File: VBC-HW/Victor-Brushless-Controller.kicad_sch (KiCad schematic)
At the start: 79 parts, among them J1 i2c QWIIC, P1 PVDD, P2 GND, Q1 TPH4R008NH, Q2 TPH4R008NH, Q3 TPH4R008NH, Q4 TPH4R008NH, Q5 TPH4R008NH, Q6 TPH4R008NH, SW1 SW_SPST, SW2 SW_SPST, U1 DRV8305NQPHPRQ1, U2 ESP-WROOM-32E, U3 LMR14010ADDCR, U5 STLM20W87F, U6 External SPI, U7 AS5047P-ATSM_C962063

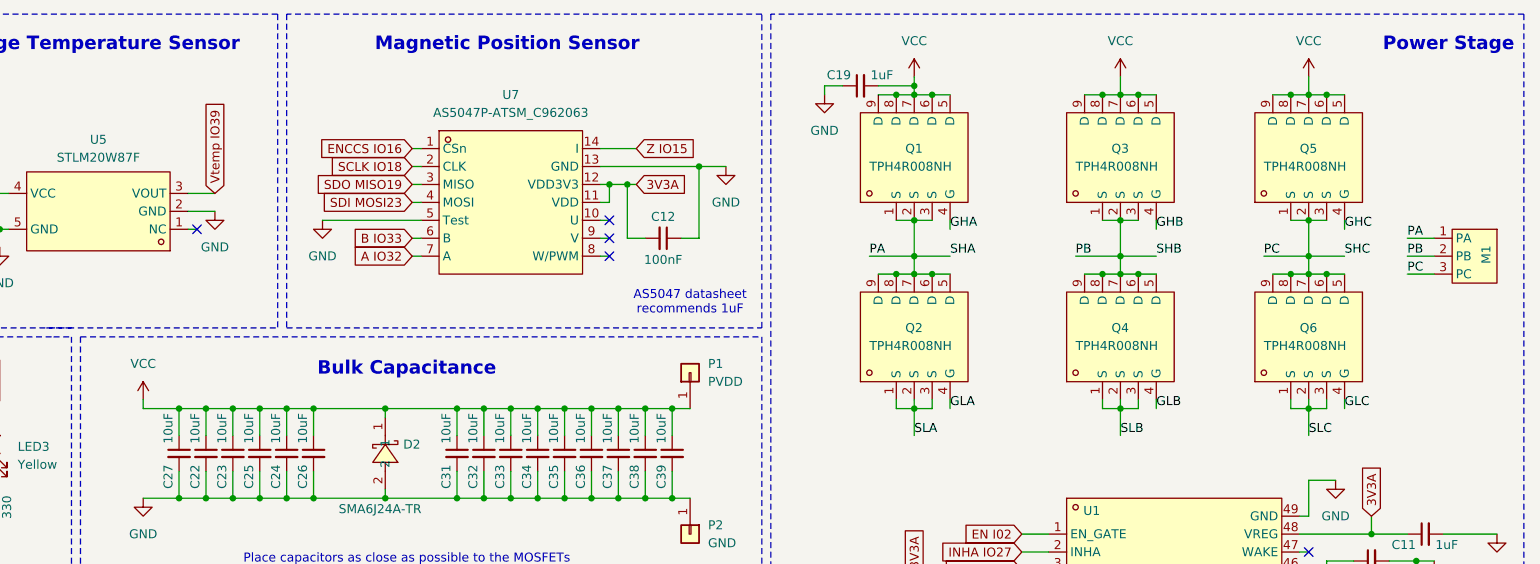
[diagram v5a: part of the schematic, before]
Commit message: Assigned external connectors
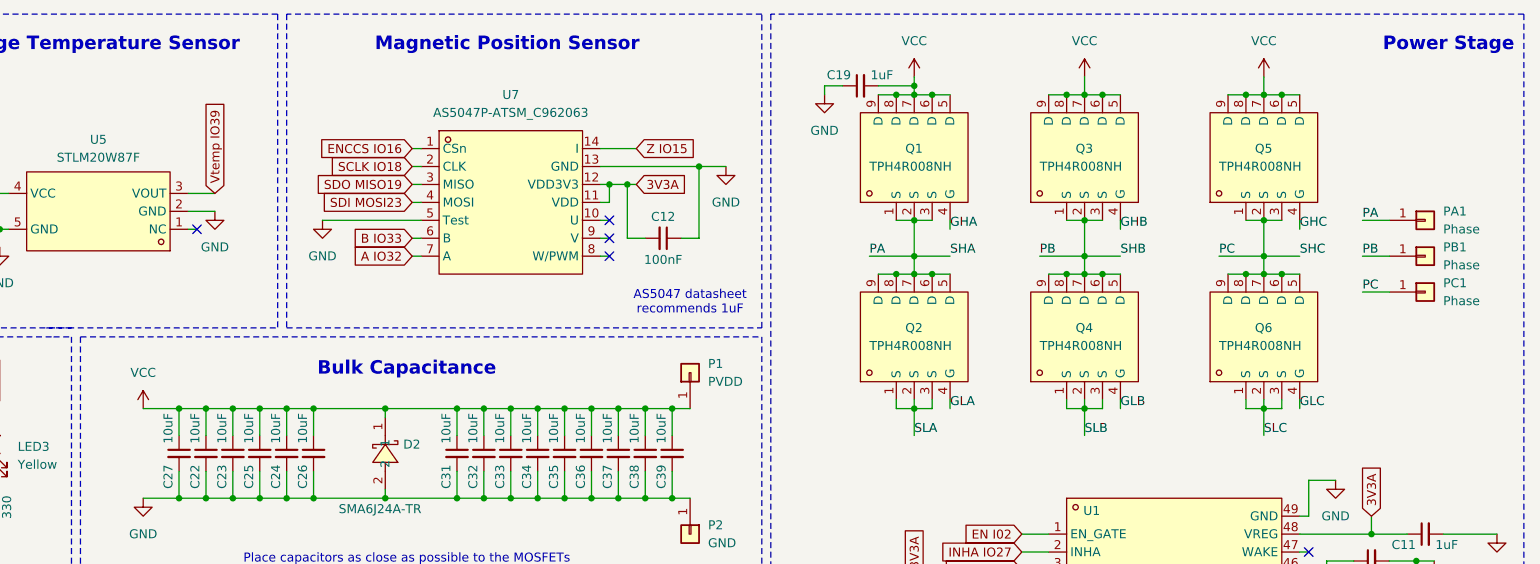
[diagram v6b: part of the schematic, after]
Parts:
- removed M1: ~, symbol BLDC_motor:BLDC_motor
- added PA1, PB1, PC1: Phase, symbol Connector_Generic:Conn_01x01
- H1: footprint (none) -> Connector_PinHeader_2.54mm:PinHeader_1x02_P2.54mm_Vertical
- H2, H3: footprint (none) -> Connector_PinHeader_2.54mm:PinHeader_1x04_P2.54mm_Vertical
- J1: footprint (none) -> Connector_JST:JST_GH_BM04B-GHS-TBT_1x04-1MP_P1.25mm_Vertical
- JP1: footprint (none) -> Jumper:SolderJumper-2_P1.3mm_Open_Pad1.0x1.5mm
- U6: footprint (none) -> Connector_JST:JST_GH_BM07B-GHS-TBT_1x07-1MP_P1.25mm_Vertical
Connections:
- net PA: now also PA1.1 (Pin_1)
- net PB: now also PB1.1 (Pin_1)
- net PC: now also PC1.1 (Pin_1)
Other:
- moved on the sheet: Q3, Q4, Q5, Q6

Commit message: Finished assigning and creating all footprints
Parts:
- P1, P2: footprint (none) -> Power_Connector:Power_Connector
- PA1: value Phase -> Phase; footprint (none) -> BLDC_Connector:BLDC_Connector
- PB1, PC1: footprint (none) -> BLDC_Connector:BLDC_Connector

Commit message: Ready to tetris
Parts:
- removed J1: i2c QWIIC, Connector_JST:JST_GH_BM04B-GHS-TBT_1x04-1MP_P1.25mm_Vertical, symbol Connector_Generic:Conn_01x04
- removed U6: External SPI, Connector_JST:JST_GH_BM07B-GHS-TBT_1x07-1MP_P1.25mm_Vertical, symbol Connector_Generic:Conn_01x08
- added J1: i2c QWIIC, Connector_JST:JST_GH_BM04B-GHS-TBT_1x04-1MP_P1.25mm_Vertical, symbol Connector_Generic:Conn_01x05
- added U6: External SPI, Connector_JST:JST_GH_BM06B-GHS-TBT_1x06-1MP_P1.25mm_Vertical, symbol Connector_Generic:Conn_01x07
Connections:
- net 3V3A: now also J1.2 (Pin_2), U6.1 (Pin_1)
- net EXTCS IO12: now also U6.3 (Pin_3)
- net GND: now also J1.1 (Pin_1), J1.MP, U6.2 (Pin_2), U6.MP
- net IO21: now also J1.3 (Pin_3)
- net IO22: now also J1.4 (Pin_4)
- net SCLK IO18: now also U6.4 (Pin_4)
- net SDI MOSI23: now also U6.5 (Pin_5)
- net SDO MISO19: now also U6.6 (Pin_6)
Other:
- moved on the sheet: H3
